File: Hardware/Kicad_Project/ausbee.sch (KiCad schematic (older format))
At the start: 0 parts

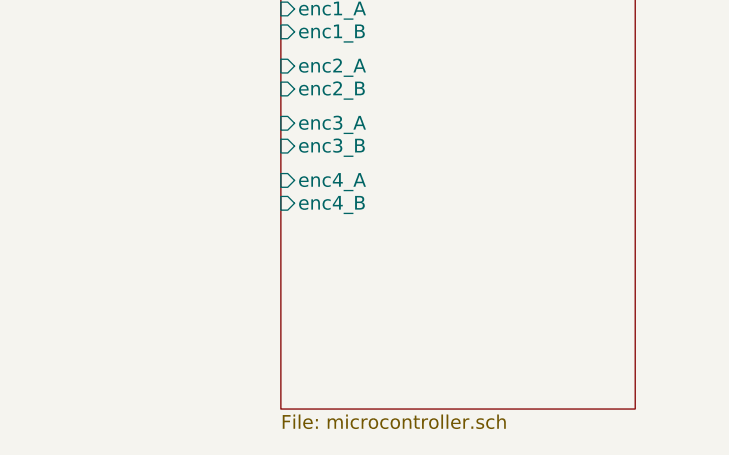
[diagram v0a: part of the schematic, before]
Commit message: [HARWARE] Add PWM definition around STM32
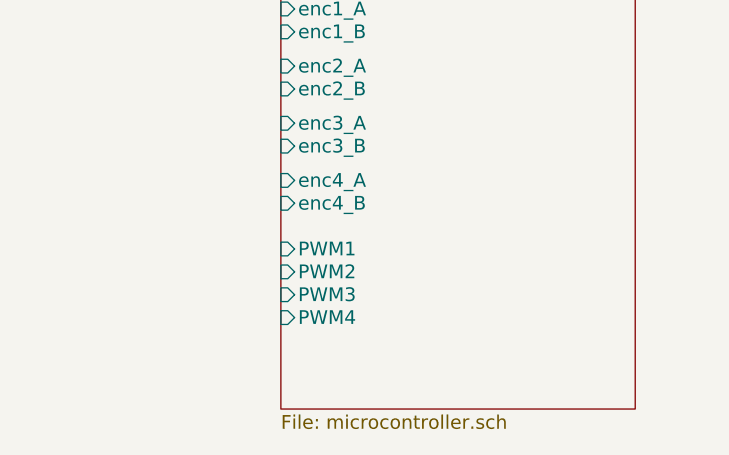
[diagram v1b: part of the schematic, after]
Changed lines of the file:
@@
-EESchema Schematic File Version 2  date dim. 06 oct. 2013 15:54:58 CEST
+EESchema Schematic File Version 2  date dim. 06 oct. 2013 18:59:37 CEST
 LIBS:power
 LIBS:device
@@
 F10 "enc1_B" I L 4250 3350 60
 F11 "enc1_A" I L 4250 3250 60
+F12 "PWM4" I L 4250 4600 60
+F13 "PWM3" I L 4250 4500 60
+F14 "PWM2" I L 4250 4400 60
+F15 "PWM1" I L 4250 4300 60
 $EndSheet
 $EndSCHEMATC

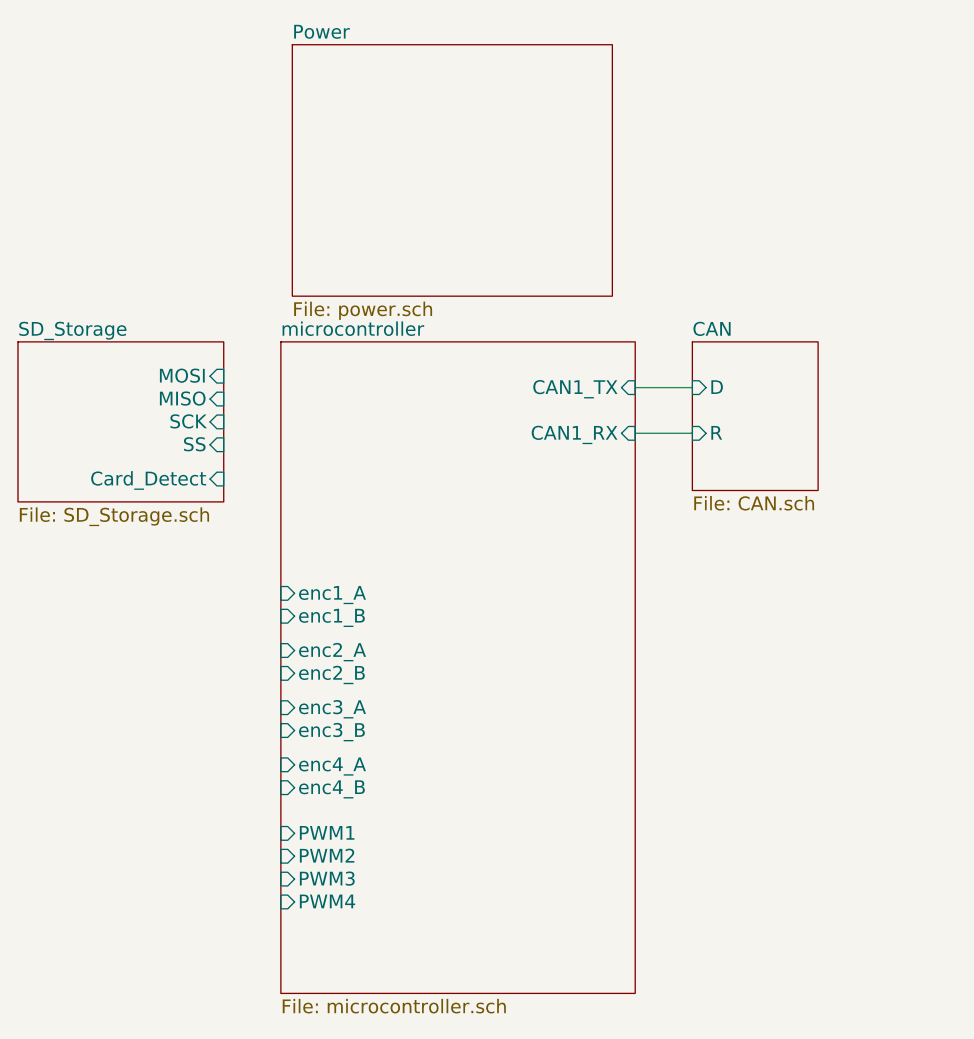
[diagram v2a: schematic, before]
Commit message: [HARWARE] Add AX12 power
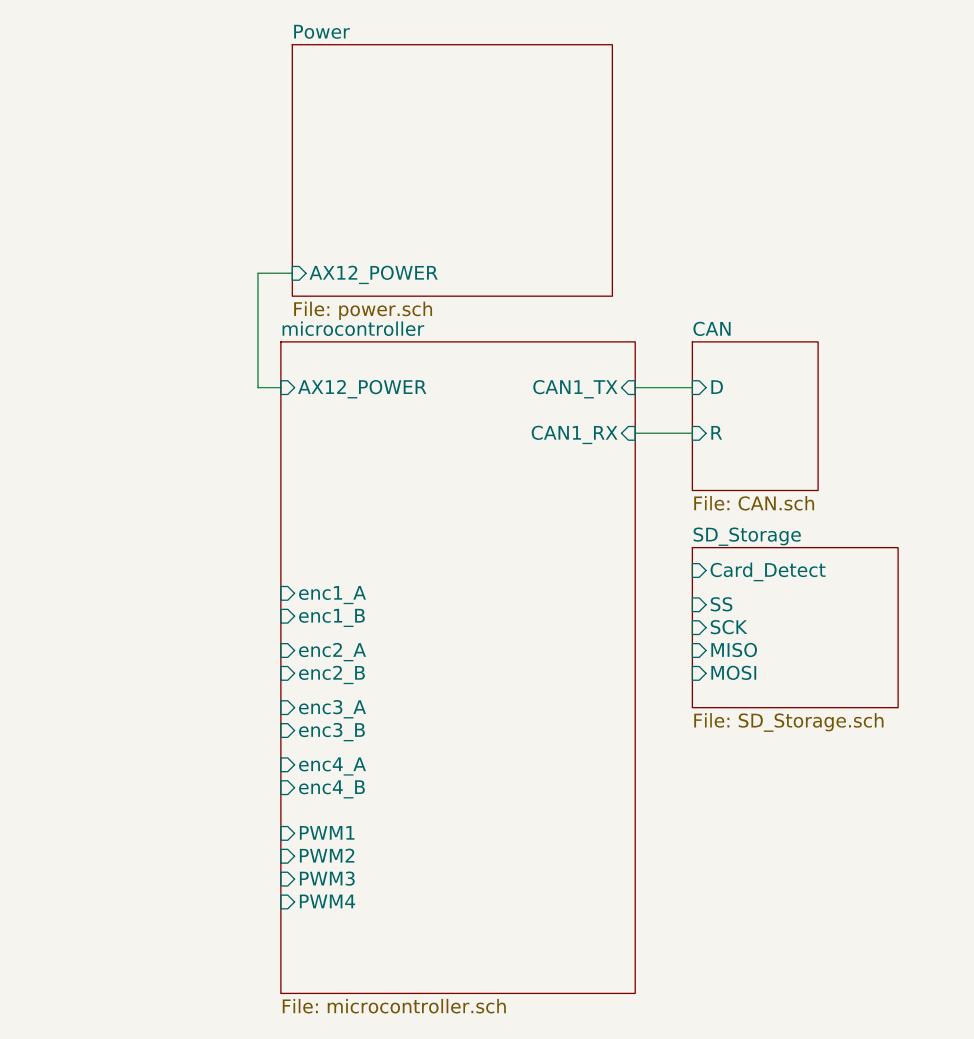
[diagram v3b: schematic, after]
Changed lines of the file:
@@
-EESchema Schematic File Version 2  date dim. 06 oct. 2013 19:04:08 CEST
+EESchema Schematic File Version 2  date dim. 06 oct. 2013 19:08:01 CEST
 LIBS:power
 LIBS:device
@@
 Comment4 ""
 $EndDescr
+Wire Wire Line
+	4250 2350 4150 2350
+Wire Wire Line
+	4150 2350 4150 1850
+Wire Wire Line
+	4150 1850 4300 1850
+Wire Wire Line
+	6050 2550 5800 2550
+Wire Wire Line
+	6050 2350 5800 2350
 $Sheet
 S 4300 850  1400 1100
@@
 F0 "Power" 60
 F1 "power.sch" 60
+F2 "AX12_POWER" I L 4300 1850 60
 $EndSheet
 $Sheet
-S 3100 2150 900  700
+S 6050 3050 900  700
 U 52514074
 F0 "SD_Storage" 60
 F1 "SD_Storage.sch" 60
-F2 "Card_Detect" I R 4000 2750 60
-F3 "MISO" I R 4000 2400 60
-F4 "SCK" I R 4000 2500 60
-F5 "MOSI" I R 4000 2300 60
-F6 "SS" I R 4000 2600 60
+F2 "Card_Detect" I L 6050 3150 60
+F3 "MISO" I L 6050 3500 60
+F4 "SCK" I L 6050 3400 60
+F5 "MOSI" I L 6050 3600 60
+F6 "SS" I L 6050 3300 60
 $EndSheet
-Wire Wire Line
-	6050 2350 5800 2350
-Wire Wire Line
-	6050 2550 5800 2550
 $Sheet
 S 6050 2150 550  650
@@
 F14 "PWM2" I L 4250 4400 60
 F15 "PWM1" I L 4250 4300 60
+F16 "AX12_POWER" I L 4250 2350 60
 $EndSheet
 $EndSCHEMATC

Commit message: [HARDWARE] Add MOSI, MISO and SCK to SD card interface
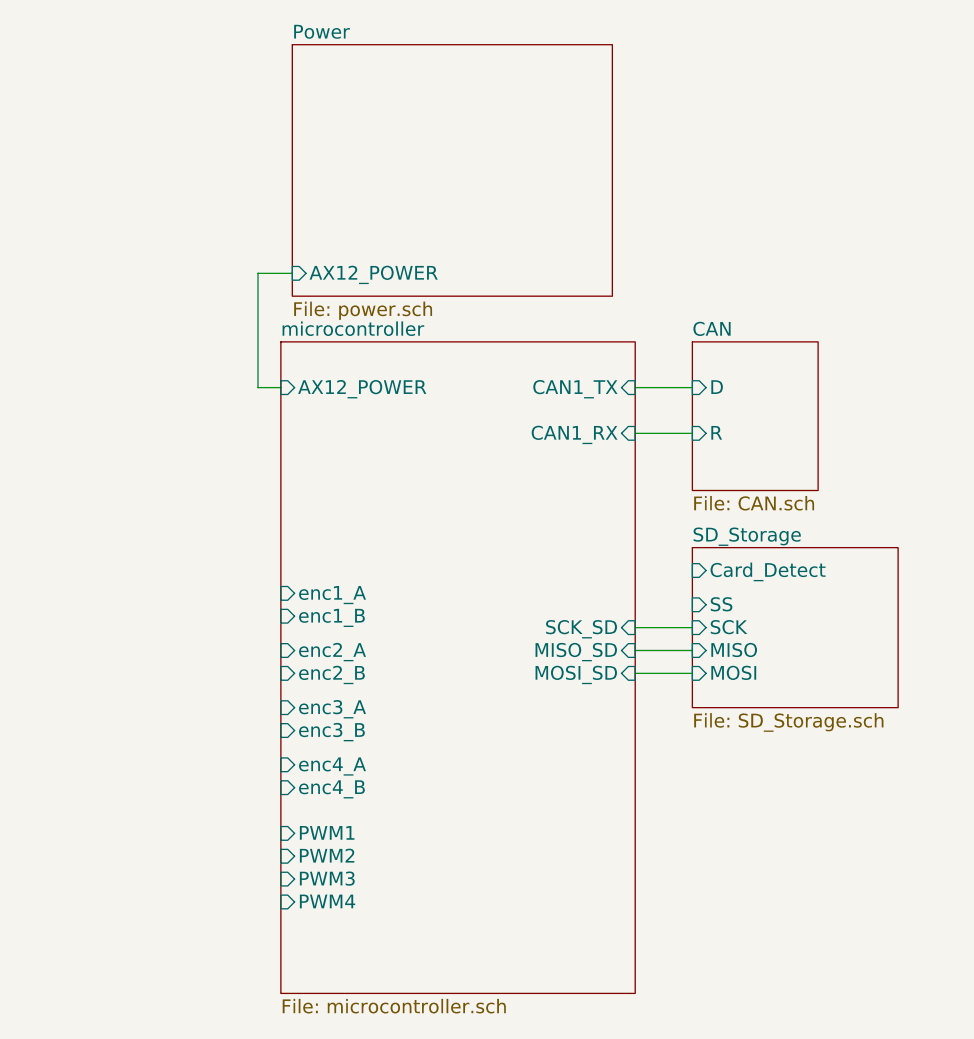
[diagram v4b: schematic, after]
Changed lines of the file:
@@
-EESchema Schematic File Version 2  date dim. 06 oct. 2013 19:08:01 CEST
+EESchema Schematic File Version 2  date dim. 06 oct. 2013 19:15:49 CEST
 LIBS:power
 LIBS:device
@@
 $EndDescr
 Wire Wire Line
-	4250 2350 4150 2350
+	6050 3600 5800 3600
 Wire Wire Line
-	4150 2350 4150 1850
+	6050 3400 5800 3400
 Wire Wire Line
-	4150 1850 4300 1850
+	6050 2350 5800 2350
 Wire Wire Line
 	6050 2550 5800 2550
 Wire Wire Line
-	6050 2350 5800 2350
+	4300 1850 4150 1850
+Wire Wire Line
+	4150 1850 4150 2350
+Wire Wire Line
+	4150 2350 4250 2350
+Wire Wire Line
+	5800 3500 6050 3500
 $Sheet
 S 4300 850  1400 1100
@@
 F15 "PWM1" I L 4250 4300 60
 F16 "AX12_POWER" I L 4250 2350 60
+F17 "SCK_SD" I R 5800 3400 60
+F18 "MOSI_SD" I R 5800 3600 60
+F19 "MISO_SD" I R 5800 3500 60
 $EndSheet
 $EndSCHEMATC

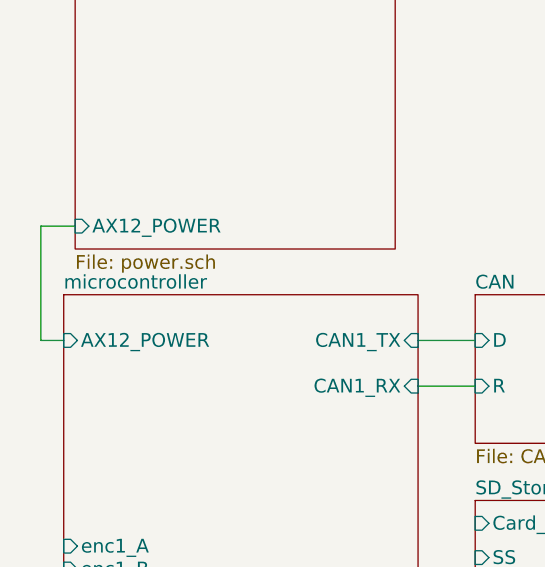
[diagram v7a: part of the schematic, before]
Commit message: [HARDWARE] Add ADC and GP2 interfaces
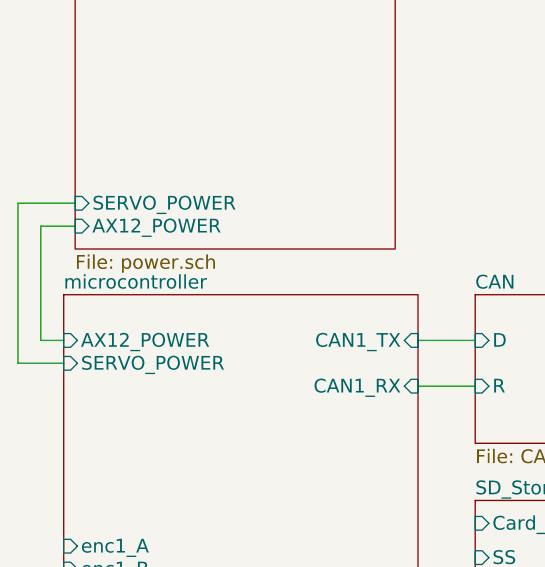
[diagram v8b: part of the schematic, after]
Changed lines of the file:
@@
-EESchema Schematic File Version 2  date dim. 06 oct. 2013 19:54:20 CEST
+EESchema Schematic File Version 2  date mar. 08 oct. 2013 19:30:07 CEST
 LIBS:power
 LIBS:device
@@
 Sheet 1 5
 Title ""
-Date "6 oct 2013"
+Date "8 oct 2013"
 Rev ""
 Comp ""
@@
 $EndDescr
 Wire Wire Line
-	6050 3600 5800 3600
+	4250 2450 4050 2450
+Wire Wire Line
+	4050 2450 4050 1750
+Wire Wire Line
+	4050 1750 4300 1750
+Wire Wire Line
+	5800 3500 6050 3500
+Wire Wire Line
+	4250 2350 4150 2350
+Wire Wire Line
+	4150 2350 4150 1850
+Wire Wire Line
+	4150 1850 4300 1850
+Wire Wire Line
+	6050 2550 5800 2550
+Wire Wire Line
+	6050 2350 5800 2350
 Wire Wire Line
 	6050 3400 5800 3400
 Wire Wire Line
-	6050 2350 5800 2350
-Wire Wire Line
-	6050 2550 5800 2550
-Wire Wire Line
-	4300 1850 4150 1850
-Wire Wire Line
-	4150 1850 4150 2350
-Wire Wire Line
-	4150 2350 4250 2350
-Wire Wire Line
-	5800 3500 6050 3500
+	6050 3600 5800 3600
 $Sheet
 S 4300 850  1400 1100
@@
 F1 "power.sch" 60
 F2 "AX12_POWER" I L 4300 1850 60
+F3 "SERVO_POWER" I L 4300 1750 60
 $EndSheet
 $Sheet
@@
 F18 "MOSI_SD" I R 5800 3600 60
 F19 "MISO_SD" I R 5800 3500 60
+F20 "SERVO_POWER" I L 4250 2450 60
 $EndSheet
 $EndSCHEMATC
